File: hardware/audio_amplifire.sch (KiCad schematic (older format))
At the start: 0 parts

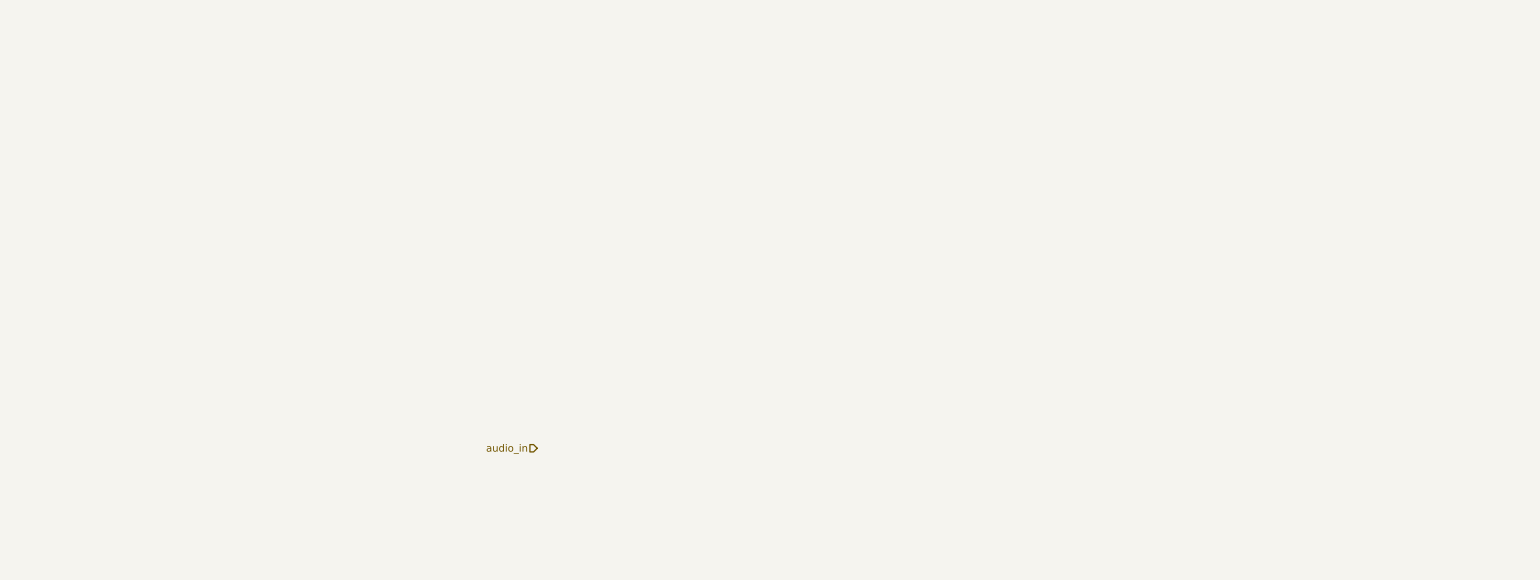
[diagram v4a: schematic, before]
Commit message: hardware: added simply class a audio amplifiere
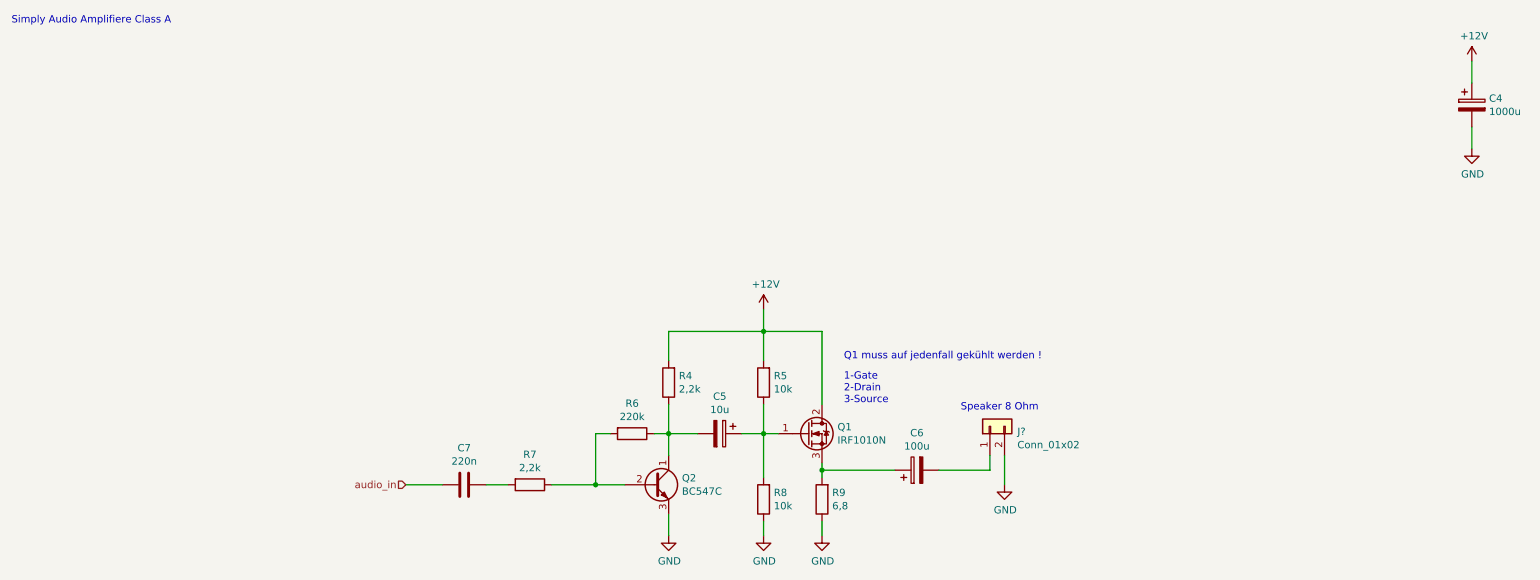
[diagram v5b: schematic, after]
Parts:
- added C4: 1000u, symbol Device:CP
- added C5: 10u, symbol Device:CP
- added C6: 100u, symbol Device:CP
- added C7: 220n, symbol Device:C
- added J?: Conn_01x02, symbol Connector_Generic:Conn_01x02
- added Q1: IRF1010N, Package_TO_SOT_THT:TO-220-3_Vertical, symbol Transistor_FET:IRF540N
- added Q2: BC547C, Package_TO_SOT_THT:TO-92_Inline, symbol Transistor_BJT:BC547
- added R4, R7: 2,2k, symbol Device:R
- added R5, R8: 10k, symbol Device:R
- added R6: 220k, symbol Device:R
- added R9: 6,8, symbol Device:R
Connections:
- net audio_in: now also C7.2
- new net: C7.1, R7.2
- new net: C5.2, Q2.1 (C), R4.1, R6.1
- new net: Q2.2 (B), R6.2, R7.1
- new net: C5.1, Q1.1 (G), R5.1, R8.2
- new net: C6.1, Q1.3 (S), R9.2
- new net: C6.2, J?.1 (Pin_1)
- new net +12V: C4.1, Q1.2 (D), R4.2, R5.2
- new net GND: C4.2, J?.2 (Pin_2), Q2.3 (E), R8.1, R9.1
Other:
- note added: "1-Gate\n2-Drain\n3-Source"
- note added: "Q1 muss auf jedenfall gekühlt werden !"
- note added: "Simply Audio Amplifiere Class A"
- note added: "Speaker 8 Ohm"

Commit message: hardware: added a 8MHz crystal with two 22pF capacitors
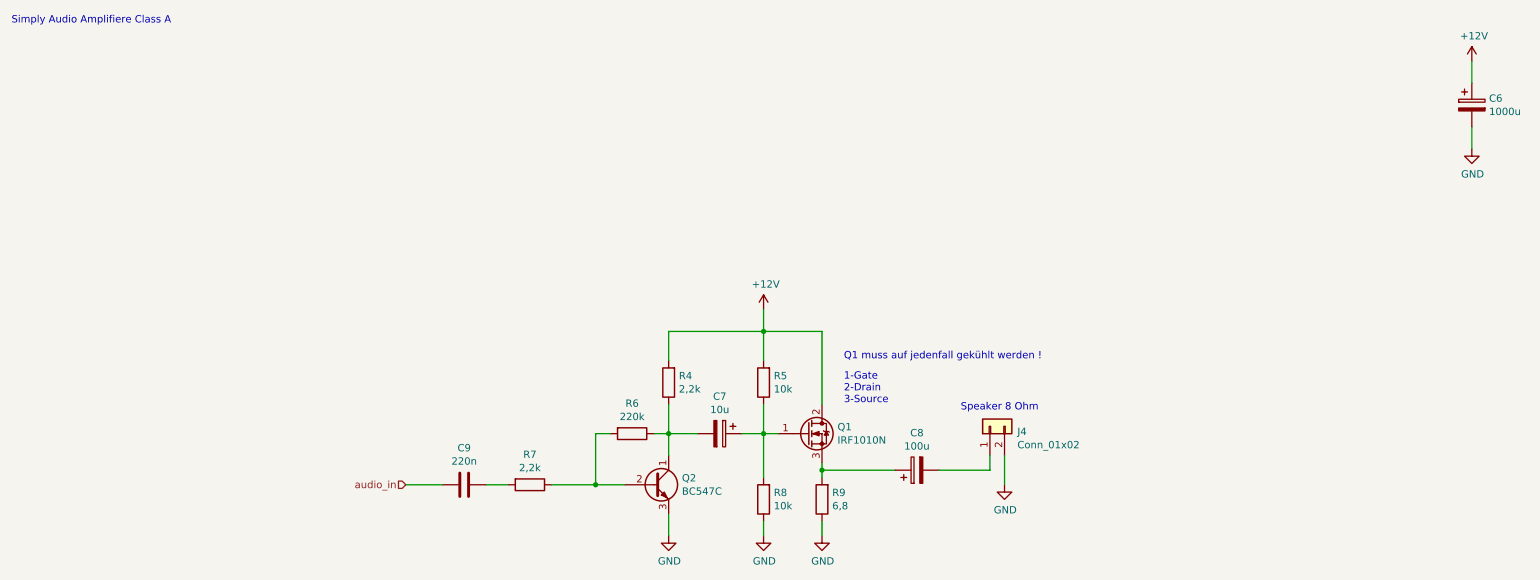
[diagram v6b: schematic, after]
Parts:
- gave numbers to parts that had none: 1
- renumbered C4 to C6, C5 to C7, C6 to C8, C7 to C9
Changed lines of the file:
@@
 Sheet 2 2
 Title "Sega Sound with SN76489AN"
-Date "2020-02-05"
+Date "2020-02-07"
 Rev "1.0"
 Comp "Thorsten Kattanek"
@@
 audio_in
 $Comp
-L Device:C C7
+L Device:C C9
 U 1 1 5E3B2D0B
 P 3750 3850
-F 0 "C7" V 3498 3850 50  0000 C CNN
+F 0 "C9" V 3498 3850 50  0000 C CNN
 F 1 "220n" V 3589 3850 50  0000 C CNN
 F 2 "" H 3788 3700 50  0001 C CNN
@@
 	4350 3850 4650 3850
 $Comp
-L power:GND #PWR024
+L power:GND #PWR025
 U 1 1 5E3B5A98
 P 5150 4200
-F 0 "#PWR024" H 5150 3950 50  0001 C CNN
+F 0 "#PWR025" H 5150 3950 50  0001 C CNN
 F 1 "GND" H 5155 4027 50  0000 C CNN
 F 2 "" H 5150 4200 50  0001 C CNN
@@
 	5150 3500 5350 3500
 $Comp
-L Device:CP C4
+L Device:CP C6
 U 1 1 5E3BBAE1
 P 10650 1250
-F 0 "C4" H 10768 1296 50  0000 L CNN
+F 0 "C6" H 10768 1296 50  0000 L CNN
 F 1 "1000u" H 10768 1205 50  0000 L CNN
 F 2 "" H 10688 1100 50  0001 C CNN
@@
 	5800 3800 5800 3500
 $Comp
-L power:GND #PWR025
+L power:GND #PWR026
 U 1 1 5E3BEBBF
 P 5800 4200
-F 0 "#PWR025" H 5800 3950 50  0001 C CNN
+F 0 "#PWR026" H 5800 3950 50  0001 C CNN
 F 1 "GND" H 5805 4027 50  0000 C CNN
 F 2 "" H 5800 4200 50  0001 C CNN
@@
 	5800 4200 5800 4100
 $Comp
-L power:+12V #PWR022
+L power:+12V #PWR023
 U 1 1 5E3BF36D
 P 5800 2650
-F 0 "#PWR022" H 5800 2500 50  0001 C CNN
+F 0 "#PWR023" H 5800 2500 50  0001 C CNN
 F 1 "+12V" H 5815 2823 50  0000 C CNN
 F 2 "" H 5800 2650 50  0001 C CNN
@@
 	6200 3700 6200 3750
 $Comp
-L power:GND #PWR026
+L power:GND #PWR027
 U 1 1 5E3C0D77
 P 6200 4200
-F 0 "#PWR026" H 6200 3950 50  0001 C CNN
+F 0 "#PWR027" H 6200 3950 50  0001 C CNN
 F 1 "GND" H 6205 4027 50  0000 C CNN
 F 2 "" H 6200 4200 50  0001 C CNN
@@
 	6200 4100 6200 4200
 $Comp
-L Device:CP C6
+L Device:CP C8
 U 1 1 5E3C1487
 P 6850 3750
-F 0 "C6" V 7105 3750 50  0000 C CNN
+F 0 "C8" V 7105 3750 50  0000 C CNN
 F 1 "100u" V 7014 3750 50  0000 C CNN
 F 2 "" H 6888 3600 50  0001 C CNN
@@
 	7350 3750 7350 3650
 $Comp
-L power:GND #PWR023
+L power:GND #PWR024
 U 1 1 5E3C4917
 P 7450 3850
-F 0 "#PWR023" H 7450 3600 50  0001 C CNN
+F 0 "#PWR024" H 7450 3600 50  0001 C CNN
 F 1 "GND" H 7455 3677 50  0000 C CNN
 F 2 "" H 7450 3850 50  0001 C CNN
@@
 	7450 3650 7450 3850
 $Comp
-L power:GND #PWR021
+L power:GND #PWR022
 U 1 1 5E3CAF25
 P 10650 1550
-F 0 "#PWR021" H 10650 1300 50  0001 C CNN
+F 0 "#PWR022" H 10650 1300 50  0001 C CNN
 F 1 "GND" H 10655 1377 50  0000 C CNN
 F 2 "" H 10650 1550 50  0001 C CNN
@@
 $EndComp
 $Comp
-L power:+12V #PWR020
+L power:+12V #PWR021
 U 1 1 5E3CB209
 P 10650 950
-F 0 "#PWR020" H 10650 800 50  0001 C CNN
+F 0 "#PWR021" H 10650 800 50  0001 C CNN
 F 1 "+12V" H 10665 1123 50  0000 C CNN
 F 2 "" H 10650 950 50  0001 C CNN
@@
 	10650 1400 10650 1550
 $Comp
-L Device:CP C5
+L Device:CP C7
 U 1 1 5E3CCE91
 P 5500 3500
-F 0 "C5" V 5245 3500 50  0000 C CNN
+F 0 "C7" V 5245 3500 50  0000 C CNN
 F 1 "10u" V 5336 3500 50  0000 C CNN
 F 2 "" H 5538 3350 50  0001 C CNN
@@
 Q1 muss auf jedenfall gekühlt werden !
 $Comp
-L Connector_Generic:Conn_01x02 J?
+L Connector_Generic:Conn_01x02 J4
 U 1 1 5E3DDFDA
 P 7350 3450
-F 0 "J?" V 7314 3262 50  0000 R CNN
+F 0 "J4" V 7314 3262 50  0000 R CNN
 F 1 "Conn_01x02" V 7223 3262 50  0000 R CNN
 F 2 "" H 7350 3450 50  0001 C CNN
